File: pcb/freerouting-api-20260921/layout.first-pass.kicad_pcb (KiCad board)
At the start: 4 copper layers, 36 x 76 mm, 115 parts, among them J1 B2B-PH-K-S, J3 B2B-PH-K-S, J4 104031-0811, Q1 AO3400A, Q2 AO3400A, SW1 PTS841GKSMTR LFS, SW2 JS202011AQN, U1 113991114, U10 SN74CBTLV3245APWR, U11 SN74CBTLV3245APWR, U3 MAX17048G+T10, U4 BMI270, U5 TPS61023DRLR, U6 AP2112K-3.3TRG1, U7 TPS22918DBVR, U8 TPS22918DBVR, U9 TPS22918DBVR

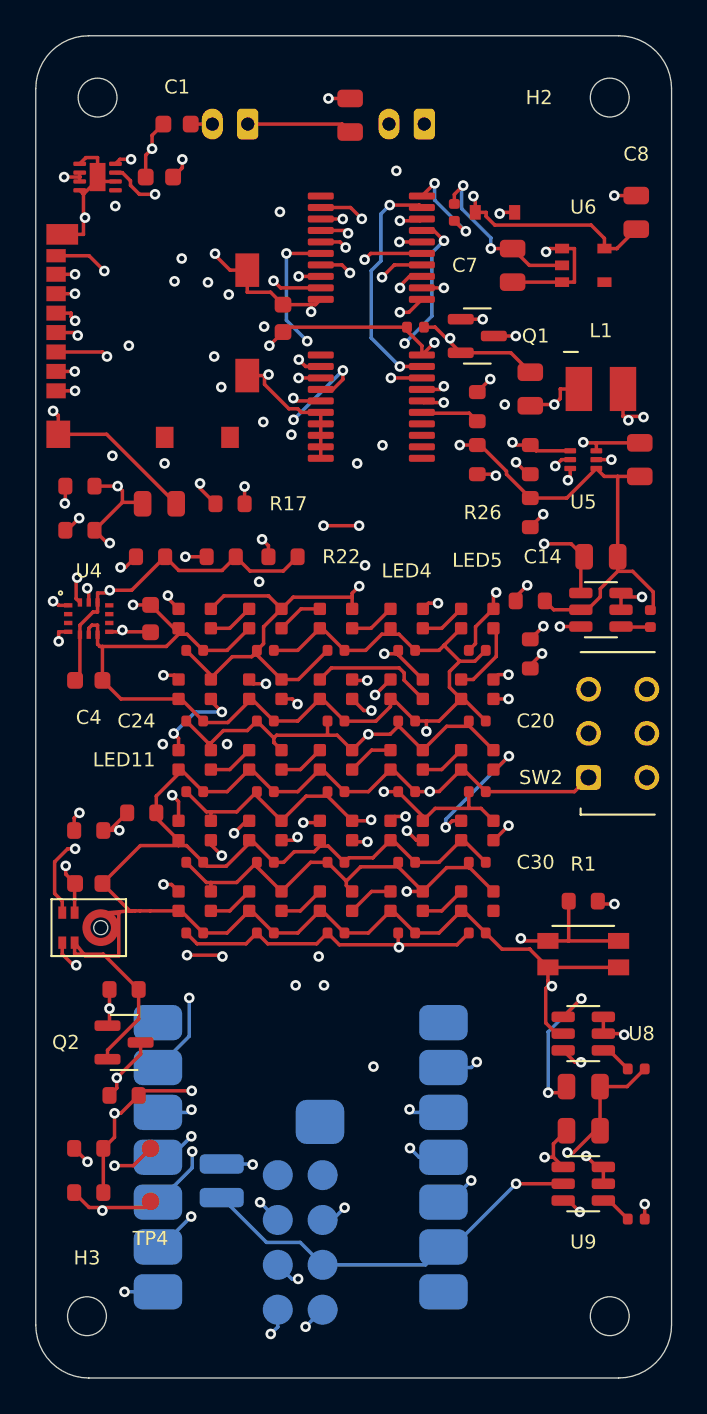
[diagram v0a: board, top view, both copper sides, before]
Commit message: Update board configuration, BOM, and documentation for new XIAO ESP32S3
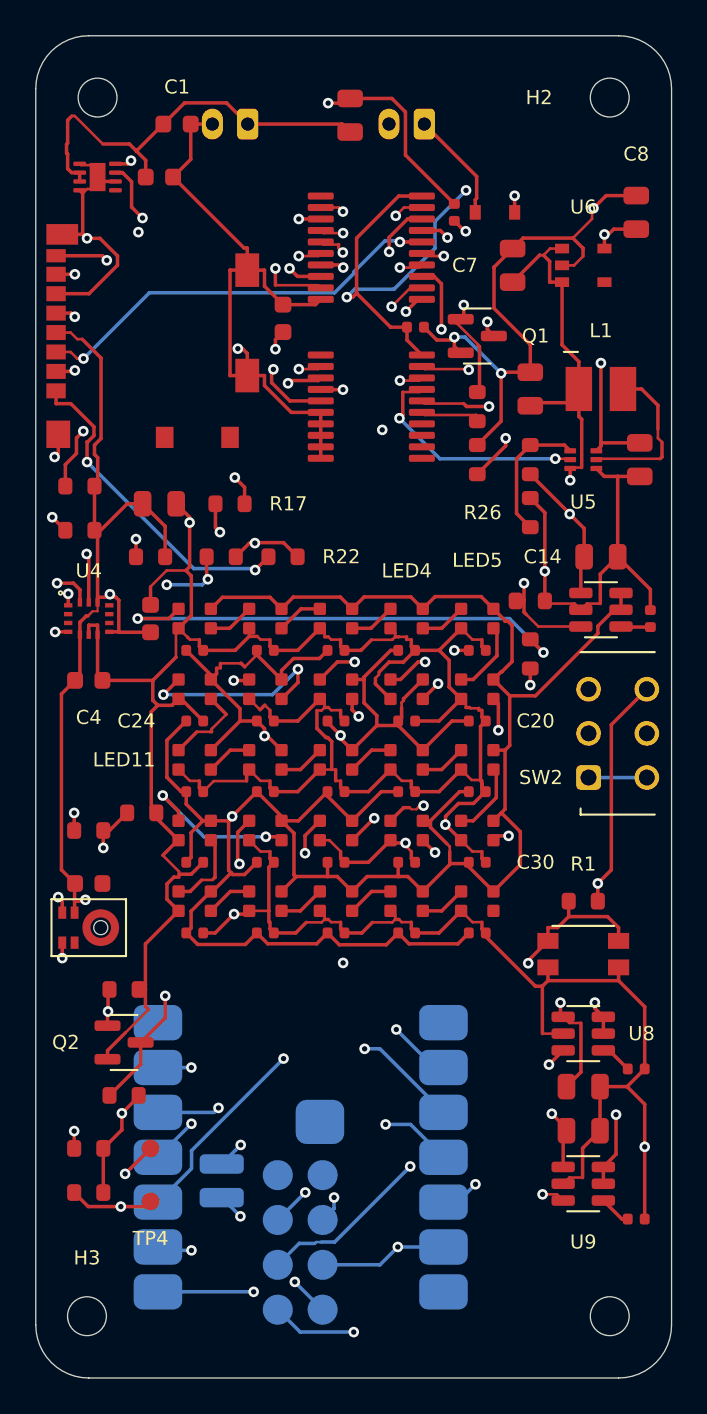
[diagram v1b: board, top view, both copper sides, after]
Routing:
- net GND: track 412.7 -> 470.9 mm, vias 21 -> 16
- net FG_SDA: track 92.1 -> 59.5 mm, vias 7 -> 6
- net LED_5V: track 175.9 -> 190.1 mm, vias 12 -> 4
- net V3V3: track 148.5 -> 160.2 mm, vias 14 -> 9
- net ISOLATE_N: track 73.0 -> 64.7 mm, vias 4 -> 3
- net SD_CLK: track 22.7 -> 15.7 mm, vias 3 -> 2
- net PDM_CLK_MCU: track 48.1 -> 41.7 mm, vias 4 -> 2
- net HOST_PDM_CLK: track 63.5 -> 57.2 mm, vias 7 -> 2
- net FG_SCL: track 86.8 -> 92.9 mm, vias 5 -> 4
- net BOOST_5V: track 19.0 -> 24.6 mm, vias 3 -> 2
- net VBAT_PERIPH: track 67.3 -> 62.3 mm, vias 4 -> 2
- net MOTOR_3V3: track 17.1 -> 21.9 mm
- net HOST_IMU_INT: track 60.2 -> 55.7 mm
- net PDM_DATA: track 50.6 -> 46.0 mm, vias 6 -> 2
- net V3V3_AON: track 37.7 -> 42.1 mm, vias 4 -> 3
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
